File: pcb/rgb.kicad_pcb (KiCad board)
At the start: 2 copper layers, 58 x 48 mm, 57 parts, among them J1 Conn_02x08_Odd_Even, J3 B4PS-VH, J4 TYPE-C-31-M-12, J5 TF-01A, J7 B4PS-VH, U1 SY8286ARAC, U2 SY8286ARAC, U4 WIFI, U5 ESP32-WROOM-32E, U7 CH340C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

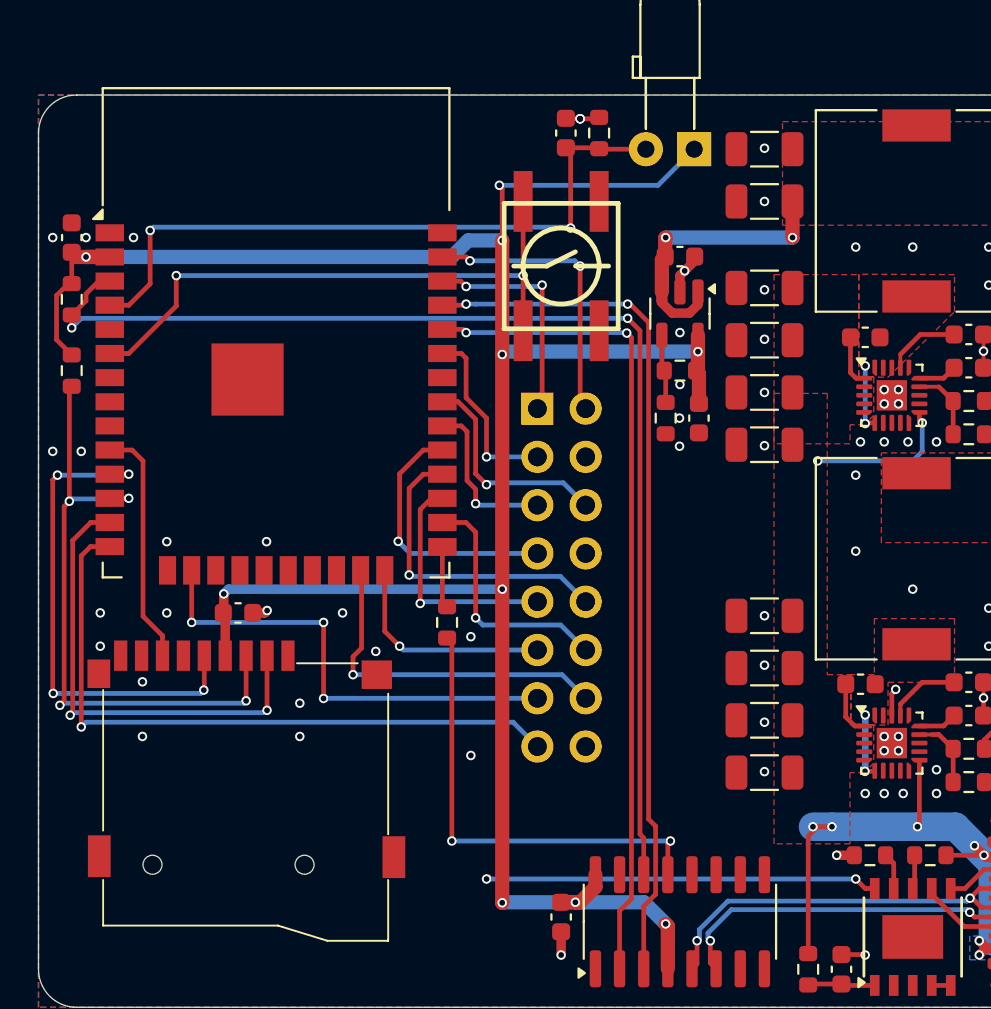
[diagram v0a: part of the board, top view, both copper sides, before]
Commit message: put a cool pattern on the bottom silk
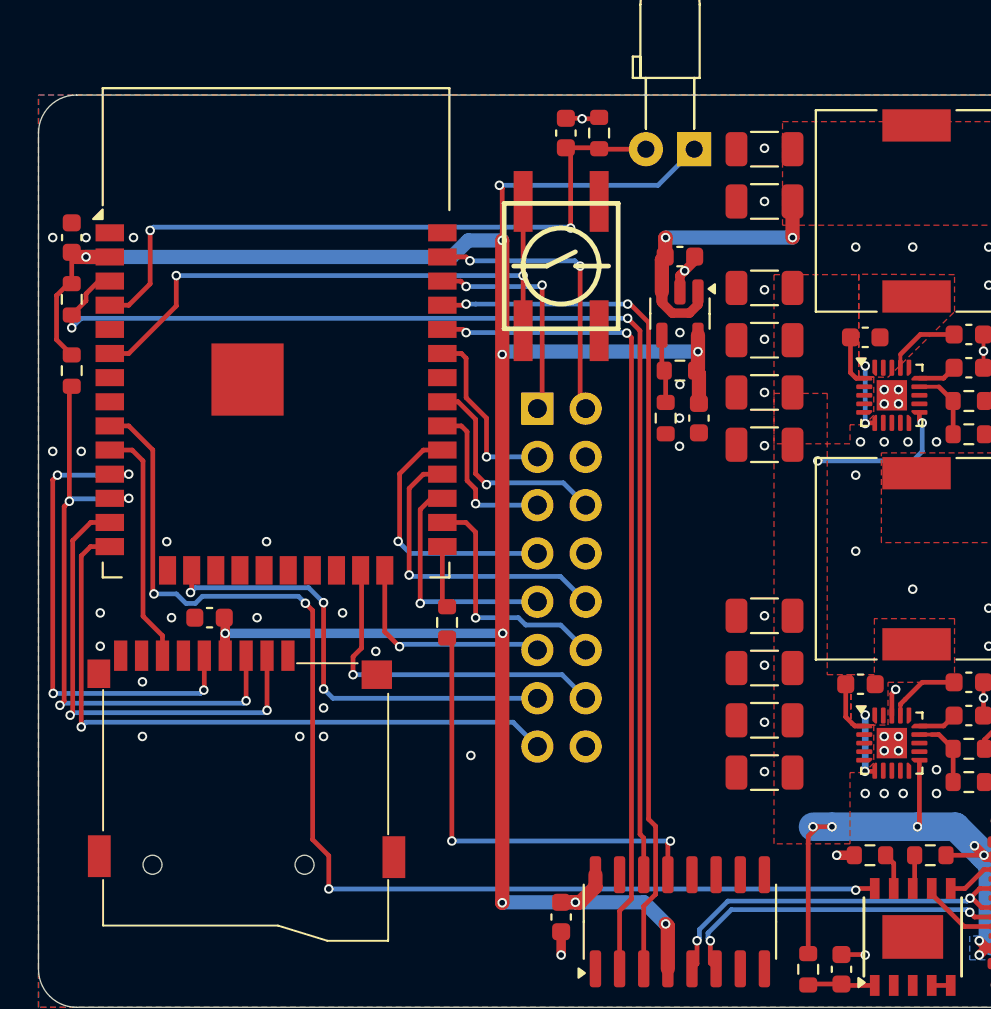
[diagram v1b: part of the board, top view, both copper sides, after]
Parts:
- moved C4 1.52 mm to (53.0, 102.5), turned to 180 degrees
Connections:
- U5 pad 9: unconnected-(U5-IO33-Pad9) -> /pd_bad
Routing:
- net /pd_bad: track 20.8 -> 63.2 mm, vias 2 -> 4
- net GND: track 17.0 -> 16.2 mm, vias 76 -> 75

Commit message: polish
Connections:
- J1 pad 8: GND -> /E
- U5 pad 8: unconnected-(U5-IO32-Pad8) -> /E
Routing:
- net /E: track 0.00 -> 31.1 mm, vias 0 -> 1
- net GND: vias 75 -> 79
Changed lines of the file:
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@@
 	(net 78 "unconnected-(U9-CFG3-Pad3)")
 	(net 79 "unconnected-(U9-CFG2-Pad2)")
-	(net 80 "unconnected-(U5-IO32-Pad8)")
+	(net 80 "/E")
 	(net 81 "unconnected-(U5-IO35-Pad7)")
 	(footprint "Connector_USB:USB_C_Receptacle_GCT_USB4105-xx-A_16P_TopMnt_Horizontal"
@@
 			(size 1.5 0.9)
 			(layers "F.Cu" "F.Paste" "F.Mask")
-			(net 80 "unconnected-(U5-IO32-Pad8)")
+			(net 80 "/E")
 			(pinfunction "IO32")
-			(pintype "bidirectional+no_connect")
+			(pintype "bidirectional")
 		)
 		(pad "9" smd rect
@@
 		(tags "capacitor")
 		(property "Reference" "C4"
-			(at 0 -1.43 360)
+			(at 0 -1.43 0)
 			(layer "F.SilkS")
 			(hide yes)
@@
 		)
 		(property "Value" "2u2"
-			(at 0 1.43 360)
+			(at 0 1.43 0)
 			(layer "F.Fab")
 			(effects
@@
 		)
 		(fp_text user "${REFERENCE}"
-			(at 0 0 360)
+			(at 0 0 0)
 			(layer "F.Fab")
 			(effects
@@
 			(layers "*.Cu" "*.Mask")
 			(remove_unused_layers no)
-			(net 4 "GND")
+			(net 80 "/E")
 			(pinfunction "Pin_8")
 			(pintype "passive")
@@
 	)
 	(via
+		(at 62.25 97)
+		(size 0.5)
+		(drill 0.3)
+		(layers "F.Cu" "B.Cu")
+		(free yes)
+		(net 4)
+	)
+	(via
 		(at 88.5 108.75)
 		(size 0.5)
@@
 	)
 	(via
+		(at 62.25 98.5)
+		(size 0.5)
+		(drill 0.3)
+		(layers "F.Cu" "B.Cu")
+		(free yes)
+		(net 4)
+	)
+	(via
 		(at 89.75 93.25)
 		(size 0.5)
@@
 	)
 	(via
+		(at 51.25 97)
+		(size 0.5)
+		(drill 0.3)
+		(layers "F.Cu" "B.Cu")
+		(free yes)
+		(net 4)
+	)
+	(via
 		(at 82.2 93.45)
 		(size 0.5)
@@
 	)
 	(via
+		(at 56 97)
+		(size 0.5)
+		(drill 0.3)
+		(layers "F.Cu" "B.Cu")
+		(free yes)
+		(net 4)
+	)
+	(via
 		(at 88.5 91.25)
 		(size 0.5)
@@
 	)
 	(segment
-		(start 62.925 98.484851)
-		(end 63 98.409851)
+		(start 63 98.819642)
+		(end 63 94.93)
 		(width 0.25)
 		(layer "F.Cu")
@@
 	)
 	(segment
-		(start 64.25 93.68)
-		(end 65.25 93.68)
+		(start 63 94.93)
+		(end 64.25 93.68)
 		(width 0.25)
 		(layer "F.Cu")
@@
 	)
 	(segment
-		(start 63 98.409851)
-		(end 63 94.93)
+		(start 64.25 93.68)
+		(end 65.25 93.68)
 		(width 0.25)
 		(layer "F.Cu")
@@
 	)
 	(segment
-		(start 63 94.93)
-		(end 64.25 93.68)
+		(start 62.928198 98.891444)
+		(end 63 98.819642)
 		(width 0.25)
 		(layer "F.Cu")
@@
 	)
 	(via
-		(at 62.925 98.484851)
+		(at 62.928198 98.891444)
 		(size 0.5)
 		(drill 0.3)
@@
 	)
 	(segment
-		(start 62.925 98.484851)
-		(end 63.560149 99.12)
+		(start 70.38 99.12)
+		(end 70.25 99.12)
 		(width 0.25)
 		(layer "B.Cu")
@@
 	)
 	(segment
-		(start 63.560149 99.12)
+		(start 63.156754 99.12)
 		(end 70.38 99.12)
 		(width 0.25)
@@
 	)
 	(segment
-		(start 70.38 99.12)
-		(end 70.25 99.12)
+		(start 62.928198 98.891444)
+		(end 63.156754 99.12)
 		(width 0.25)
 		(layer "B.Cu")
@@
 		(net 77)
 	)
+	(segment
+		(start 50.5 93)
+		(end 48.64 91.14)
+		(width 0.25)
+		(layer "F.Cu")
+		(net 80)
+	)
+	(segment
+		(start 48.64 91.14)
+		(end 47.75 91.14)
+		(width 0.25)
+		(layer "F.Cu")
+		(net 80)
+	)
+	(segment
+		(start 50.59 97.75)
+		(end 50.5 97.66)
+		(width 0.25)
+		(layer "F.Cu")
+		(net 80)
+	)
+	(segment
+		(start 50.5 97.66)
+		(end 50.5 93)
+		(width 0.25)
+		(layer "F.Cu")
+		(net 80)
+	)
+	(via
+		(at 50.59 97.75)
+		(size 0.5)
+		(drill 0.3)
+		(layers "F.Cu" "B.Cu")
+		(net 80)
+	)
+	(segment
+		(start 71.425 97.755)
+		(end 50.595 97.755)
+		(width 0.25)
+		(layer "B.Cu")
+		(net 80)
+	)
+	(segment
+		(start 72.79 99.12)
+		(end 71.425 97.755)
+		(width 0.25)
+		(layer "B.Cu")
+		(net 80)
+	)
+	(segment
+		(start 50.595 97.755)
+		(end 50.59 97.75)
+		(width 0.25)
+		(layer "B.Cu")
+		(net 80)
+	)
 	(zone

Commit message: mostly ready for production. 18 $ / board in qty. 5
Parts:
- J1: value Conn_02x08_Odd_Even -> 2.54-2*8P
- R10: value 57k -> 56k
- U4: value WIFI -> EVQQ2
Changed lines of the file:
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@@
 			)
 		)
-		(property "Value" "WIFI"
+		(property "Value" "EVQQ2"
 			(at 0 4 -90)
 			(layer "F.Fab")
@@
 		(sheetname "Root")
 		(sheetfile "rgb.kicad_sch")
-		(attr through_hole)
+		(attr through_hole exclude_from_bom dnp)
 		(fp_line
 			(start -1.33 1.27)
@@
 		(sheetname "Root")
 		(sheetfile "rgb.kicad_sch")
-		(attr through_hole)
+		(attr through_hole exclude_from_bom dnp)
 		(fp_line
 			(start -1.33 1.27)
@@
 			)
 		)
-		(property "Value" "57k"
+		(property "Value" "56k"
 			(at 0 1.43 180)
 			(layer "F.Fab")
@@
 			)
 		)
-		(property "Value" "Conn_02x08_Odd_Even"
+		(property "Value" "2.54-2*8P"
 			(at -1.27 -20.55 180)
 			(layer "B.Fab")

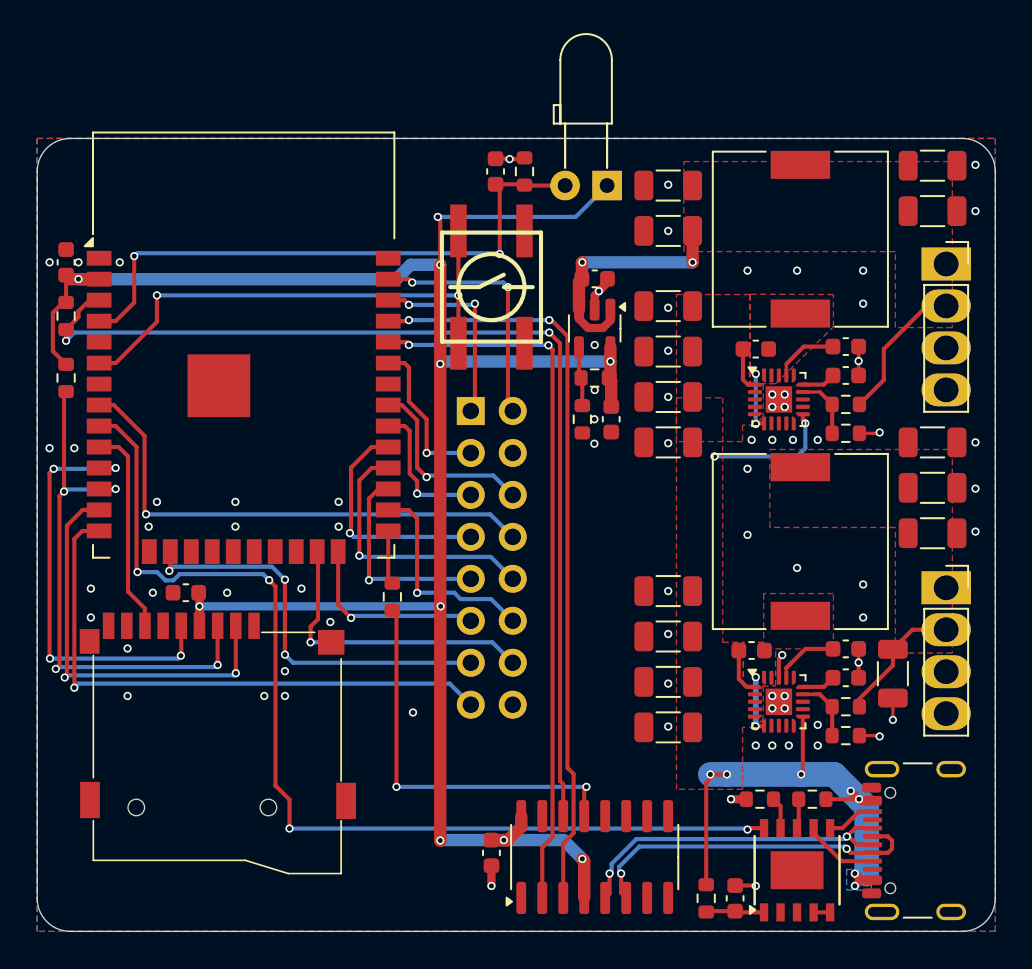
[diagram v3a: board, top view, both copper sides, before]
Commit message: add pattern to top silkscreen, order
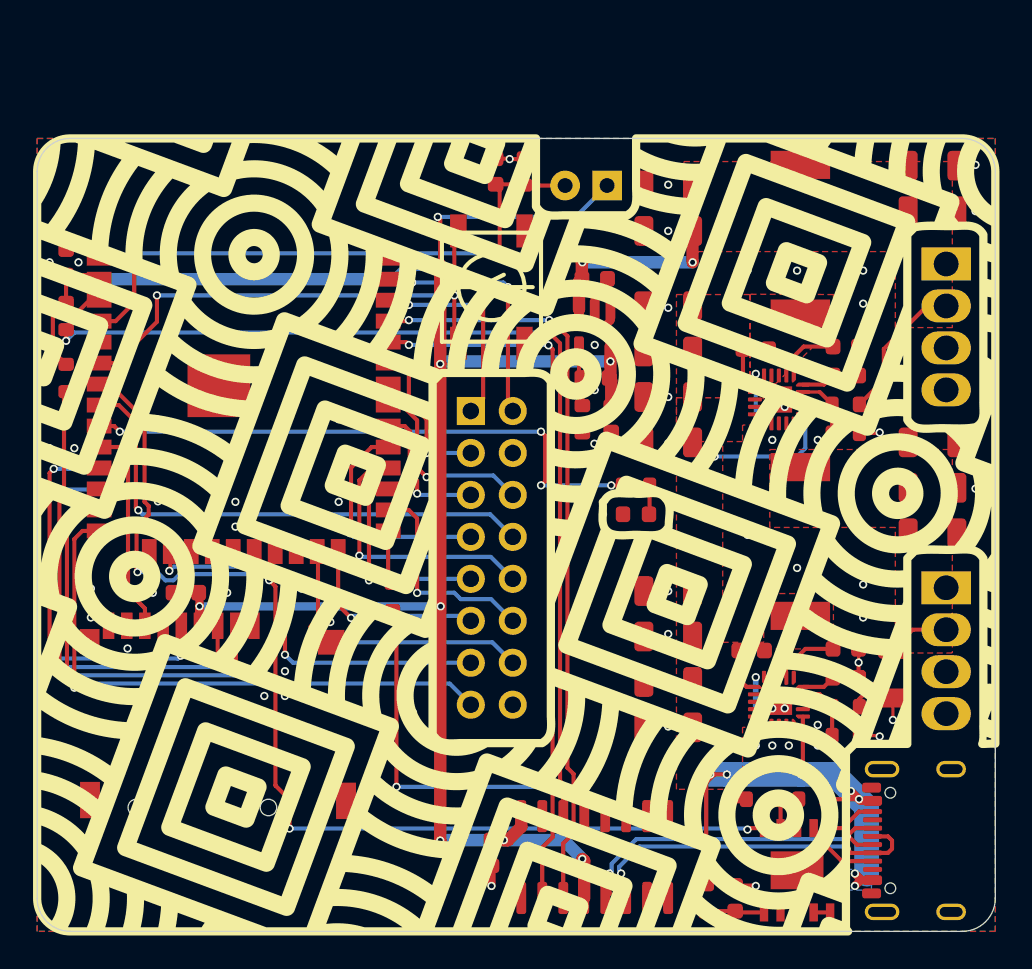
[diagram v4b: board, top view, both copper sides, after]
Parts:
- added D2: GREEN, LED_SMD:LED_0603_1608Metric, F.Cu at (80.2, 97.8)
- added R9: 1k, Resistor_SMD:R_0603_1608Metric, F.Cu at (80.2, 96.0)
- U4: value EVQQ2 -> TACTILE
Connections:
- U5 pad 7: unconnected-(U5-IO35-Pad7) -> /pd_bad
- U5 pad 9: /pd_bad -> Net-(U5-IO33)
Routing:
- net Net-(U5-IO33): track 0.00 -> 35.3 mm, vias 0 -> 4
- net /pd_bad: track 63.2 -> 66.1 mm
- net Net-(D2-A): track 0.00 -> 1.77 mm
- net /R0: track 12.0 -> 12.7 mm
- net GND: vias 79 -> 82

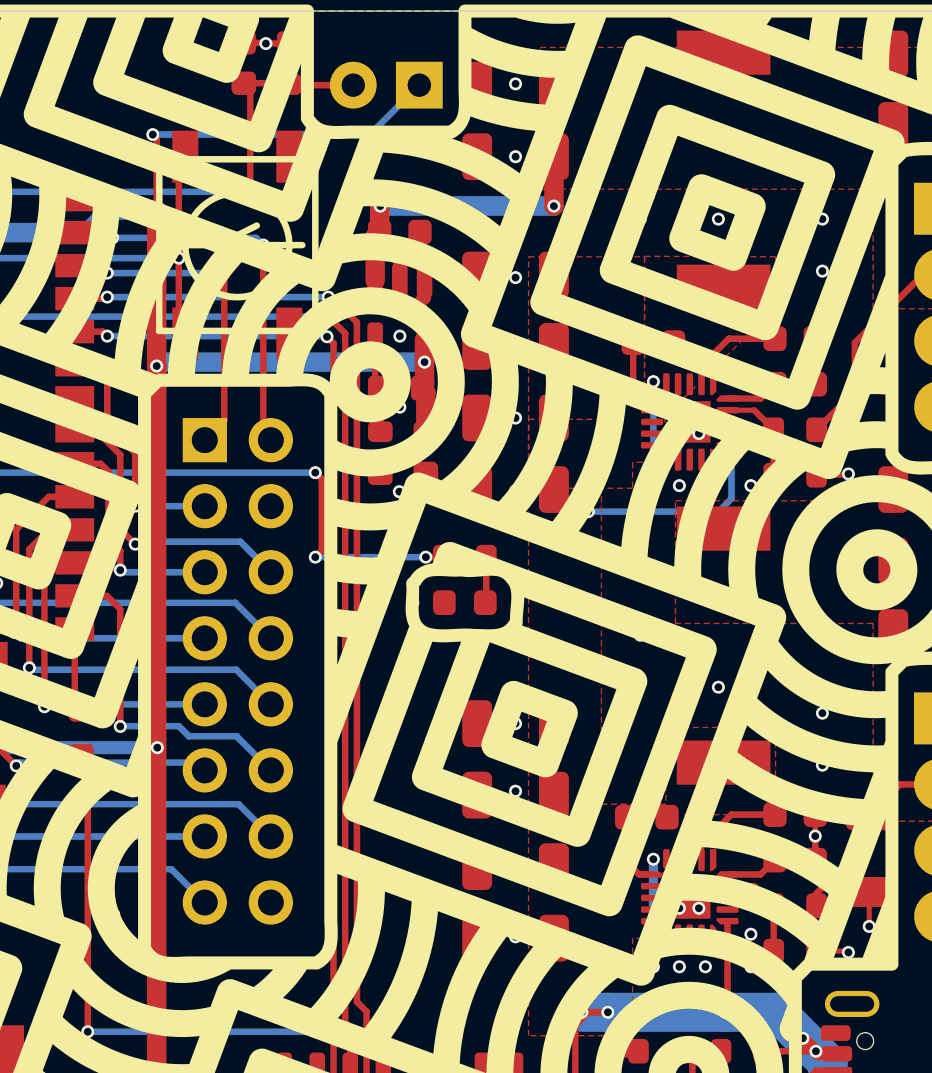
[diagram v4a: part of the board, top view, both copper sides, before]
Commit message: pcb: increase esp32 voltage slightly
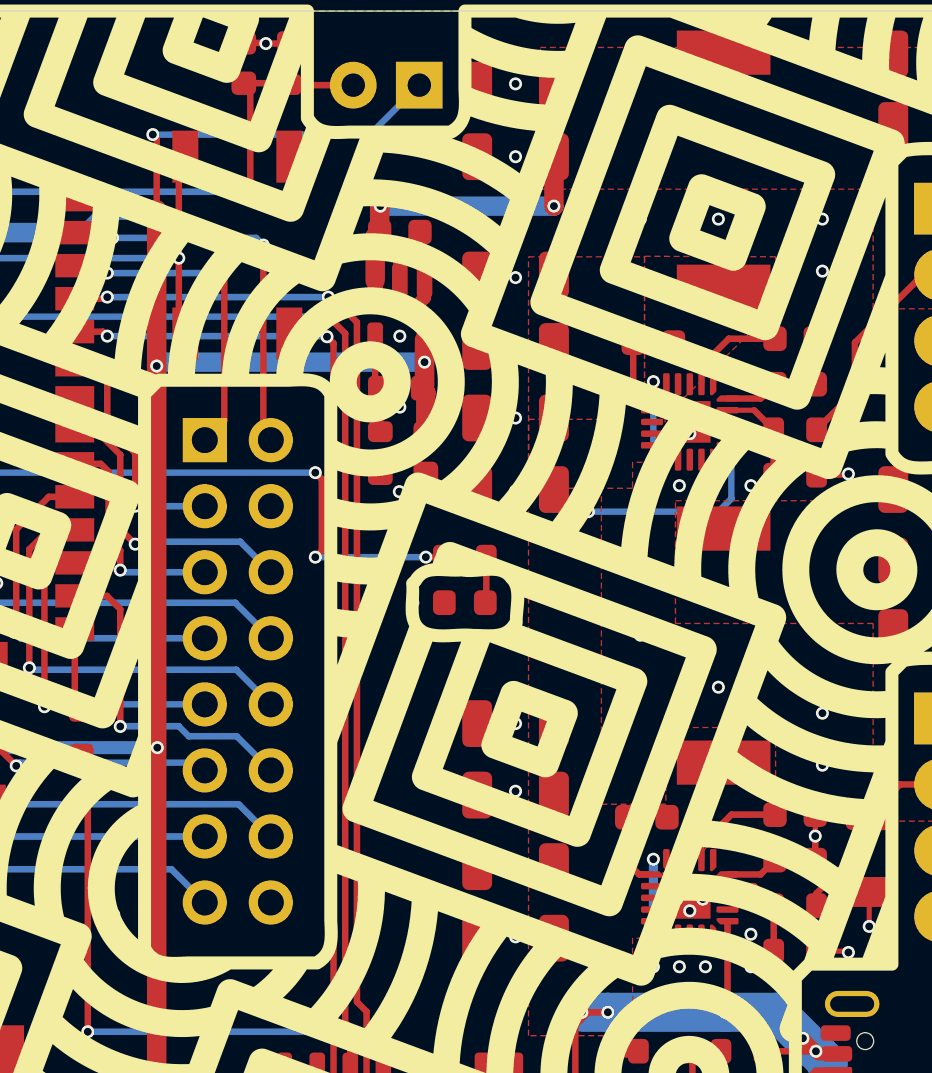
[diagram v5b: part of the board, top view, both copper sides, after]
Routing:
- net GND: track 16.2 -> 14.8 mm, vias 82 -> 81
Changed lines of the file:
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@@
 				(type solid)
 			)
-			(layer "F.SilkS")
+			(layer "Cmts.User")
 		)
 		(fp_line
@@
 				(type solid)
 			)
-			(layer "F.SilkS")
+			(layer "Cmts.User")
 		)
 		(fp_line
@@
 				(type solid)
 			)
-			(layer "F.SilkS")
+			(layer "Cmts.User")
 		)
 		(fp_line
@@
 				(type solid)
 			)
-			(layer "F.SilkS")
+			(layer "Cmts.User")
 		)
 		(fp_line
@@
 				(type solid)
 			)
-			(layer "F.SilkS")
+			(layer "Cmts.User")
 		)
 		(fp_line
@@
 				(type solid)
 			)
-			(layer "F.SilkS")
+			(layer "Cmts.User")
 		)
 		(fp_line
@@
 				(type solid)
 			)
-			(layer "F.SilkS")
+			(layer "Cmts.User")
 		)
 		(fp_circle
@@
 			)
 			(fill none)
-			(layer "F.SilkS")
+			(layer "Cmts.User")
 		)
 		(pad "A" smd rect
@@
 	)
 	(segment
-		(start 88.9 106.5)
-		(end 88.9 107.65)
-		(width 0.25)
-		(layer "F.Cu")
-		(net 4)
-	)
-	(segment
 		(start 78.525 83.5)
 		(end 78.525 83.725)
@@
 	)
 	(segment
-		(start 89.062348 106.312348)
-		(end 89.062348 106.337652)
-		(width 0.25)
-		(layer "F.Cu")
-		(net 4)
-	)
-	(segment
 		(start 86.925 115)
 		(end 86 115)
@@
 	)
 	(segment
-		(start 89.101888 106.272807)
-		(end 89.062348 106.312348)
-		(width 0.25)
-		(layer "F.Cu")
-		(net 4)
-	)
-	(segment
 		(start 93.725 106.725)
 		(end 93.725 105.9)
@@
 	)
 	(segment
-		(start 89.062348 106.337652)
-		(end 88.9 106.5)
-		(width 0.25)
-		(layer "F.Cu")
-		(net 4)
-	)
-	(segment
 		(start 71.5 119.025)
 		(end 71.5 120.25)
@@
 	)
 	(via
-		(at 89.25 108.75)
-		(size 0.5)
-		(drill 0.3)
-		(layers "F.Cu" "B.Cu")
-		(net 4)
-	)
-	(via
 		(at 66.75 109.75)
 		(size 0.5)
@@
 	)
 	(via
-		(at 95.8 110.2)
+		(at 88.9 108.65)
 		(size 0.5)
 		(drill 0.3)
@@
 	)
 	(via
-		(at 91.25 110.5)
+		(at 95.8 110.2)
 		(size 0.5)
 		(drill 0.3)
 		(layers "F.Cu" "B.Cu")
-		(free yes)
 		(net 4)
 	)
 	(via
-		(at 56 98.5)
+		(at 91.25 110.5)
 		(size 0.5)
 		(drill 0.3)
@@
 	)
 	(via
-		(at 89.101888 106.272807)
+		(at 56 98.5)
 		(size 0.5)
 		(drill 0.3)
 		(layers "F.Cu" "B.Cu")
+		(free yes)
 		(net 4)
 	)
@@
 	)
 	(via
-		(at 88.5 108.75)
+		(at 59 108.75)
 		(size 0.5)
 		(drill 0.3)
 		(layers "F.Cu" "B.Cu")
+		(free yes)
 		(net 4)
 	)
 	(via
-		(at 59 108.75)
+		(at 46.5 82.5)
 		(size 0.5)
 		(drill 0.3)
@@
 	)
 	(via
-		(at 46.5 82.5)
+		(at 62.25 98.5)
 		(size 0.5)
 		(drill 0.3)
@@
 	)
 	(via
-		(at 62.25 98.5)
+		(at 89.4 109.15)
 		(size 0.5)
 		(drill 0.3)
 		(layers "F.Cu" "B.Cu")
-		(free yes)
 		(net 4)
 	)
@@
 	)
 	(via
-		(at 89.25 91.25)
+		(at 88.9 90.3)
 		(size 0.5)
 		(drill 0.3)
@@
 	)
 	(via
+		(at 88.4 109.15)
+		(size 0.5)
+		(drill 0.3)
+		(layers "F.Cu" "B.Cu")
+		(net 4)
+	)
+	(via
 		(at 59 107.25)
 		(size 0.5)
@@
 	)
 	(via
-		(at 88.5 90.5)
+		(at 88.4 90.8)
 		(size 0.5)
 		(drill 0.3)
@@
 	)
 	(via
-		(at 89.25 90.5)
+		(at 89.4 90.8)
 		(size 0.5)
 		(drill 0.3)
@@
 	)
 	(via
-		(at 89.25 109.5)
+		(at 88.9 109.6)
 		(size 0.5)
 		(drill 0.3)
@@
 	)
 	(via
-		(at 88.5 109.5)
-		(size 0.5)
-		(drill 0.3)
-		(layers "F.Cu" "B.Cu")
-		(net 4)
-	)
-	(via
 		(at 94 102)
 		(size 0.5)
@@
 	)
 	(via
-		(at 88.5 91.25)
+		(at 88.9 91.25)
 		(size 0.5)
 		(drill 0.3)
@@
 		(polygon
 			(pts
-				(xy 88.7 108.15) (xy 88.7 105.9) (xy 92.2 105.9) (xy 92.2 102.55) (xy 87.98 102.55) (xy 87.98 105.5)
+				(xy 88.7 108.15) (xy 90.6 105.9) (xy 92.2 105.9) (xy 92.2 102.55) (xy 87.98 102.55) (xy 87.98 105.5)
 				(xy 86.75 105.5) (xy 86.73 108.15)
 			)
